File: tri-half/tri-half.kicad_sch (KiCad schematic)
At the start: 8 parts, among them J1 Conn_01x05_Pin, J2 Conn_01x05_Pin, J3 Conn_01x05_Pin

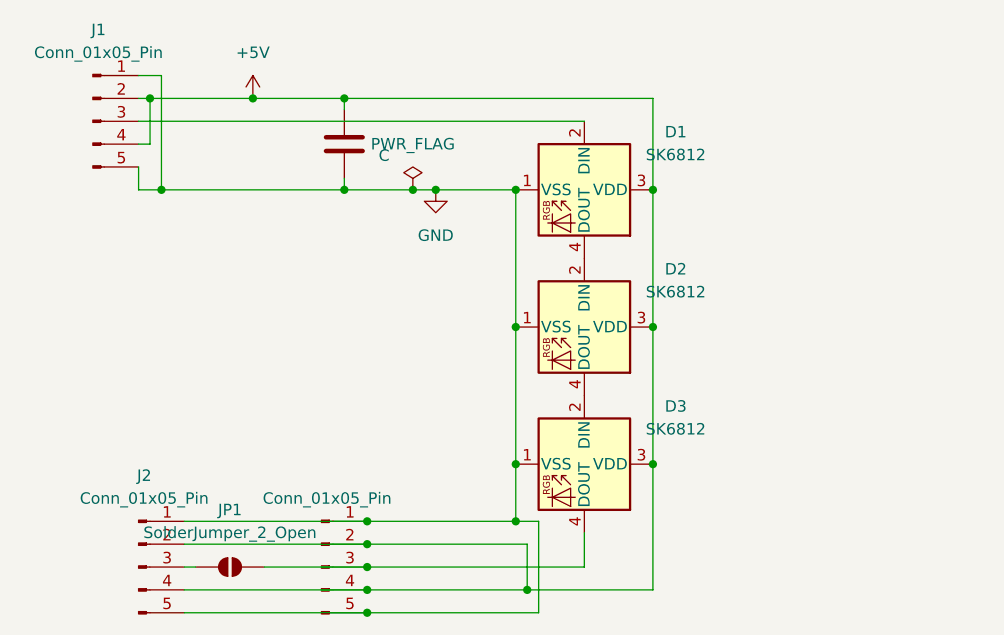
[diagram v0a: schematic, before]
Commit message: added mic to antenna, decagons, octagons and all the shenanigans
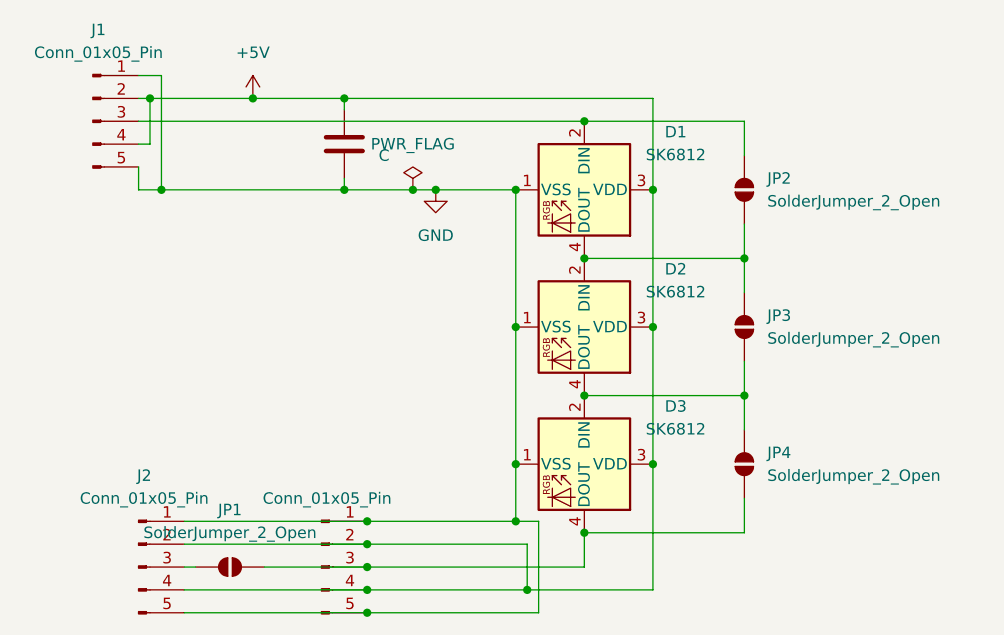
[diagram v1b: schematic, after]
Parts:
- added JP2, JP3, JP4: SolderJumper_2_Open, Jumper:SolderJumper-2_P1.3mm_Open_RoundedPad1.0x1.5mm, symbol Jumper:SolderJumper_2_Open
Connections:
- net at D1.2 (DIN), J1.3 (Pin_3): now also JP2.2 (B)
- net at D1.4 (DOUT), D2.2 (DIN): now also JP2.1 (A), JP3.2 (B)
- net at D2.4 (DOUT), D3.2 (DIN): now also JP3.1 (A), JP4.2 (B)
- net at D3.4 (DOUT), J3.3 (Pin_3), JP1.2 (B): now also JP4.1 (A)
